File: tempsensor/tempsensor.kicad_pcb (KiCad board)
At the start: 4 copper layers, 40 x 40 mm, 68 parts, among them J1 Conn_01x14, J2 Conn_01x04, J3 Conn_ARM_JTAG_SWD_10, J4 USB_B_Micro, J5 Conn_01x02, SW1 SW_DIP_x06, SW2 PW_ON, SW4 ~INT, U1 MKW41Z512VHT, U2 24C16, U3 MCP9844, U4 SN74LVC2T45DCUR, U5 SN74LVC2T45DCUR, U6 BQ24012, Y1 32MHz 10PPM SMT 2.0x1.6mm 10PF, Y2 32.768KHz 20PPM 3.2x1.5mm 7PF

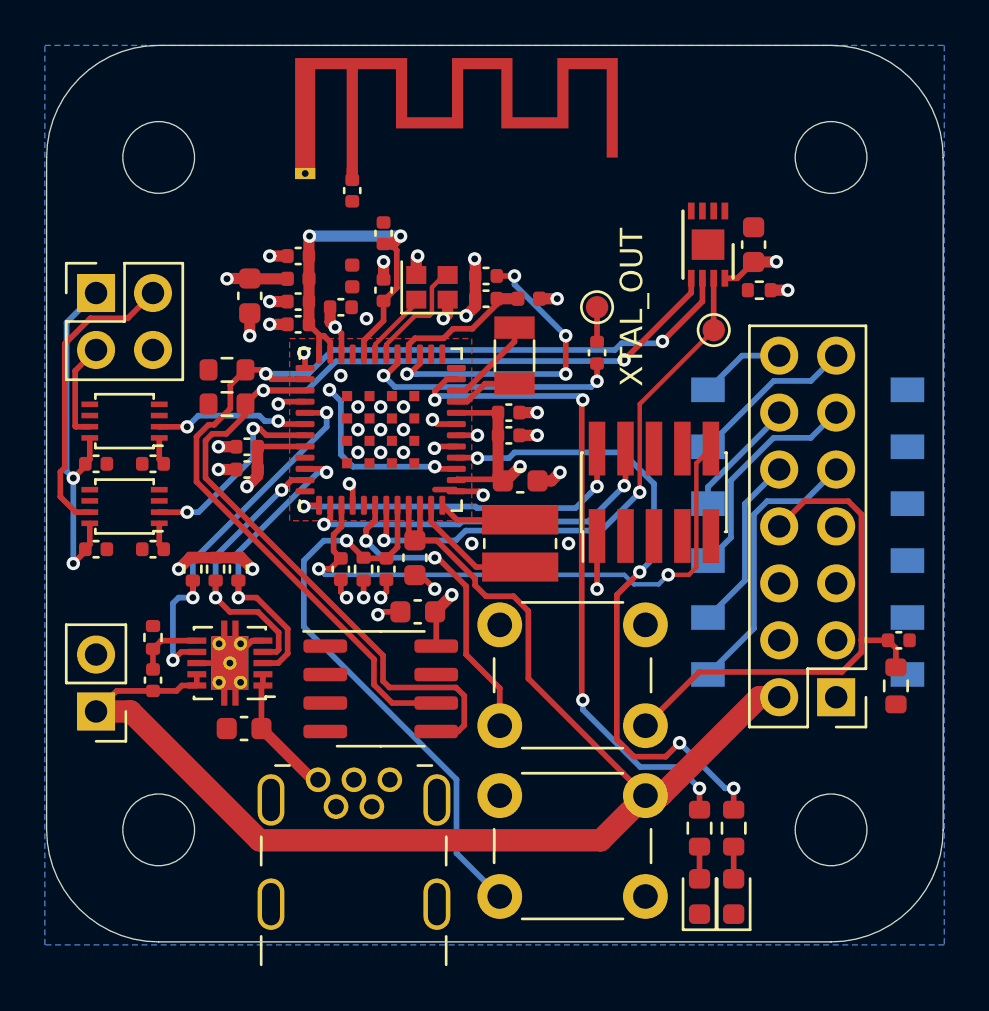
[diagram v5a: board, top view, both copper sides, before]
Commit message: Finished layouting tempsensor and thermostat. Parts are ordered from Mouser, PCB ordered from beta-layout.
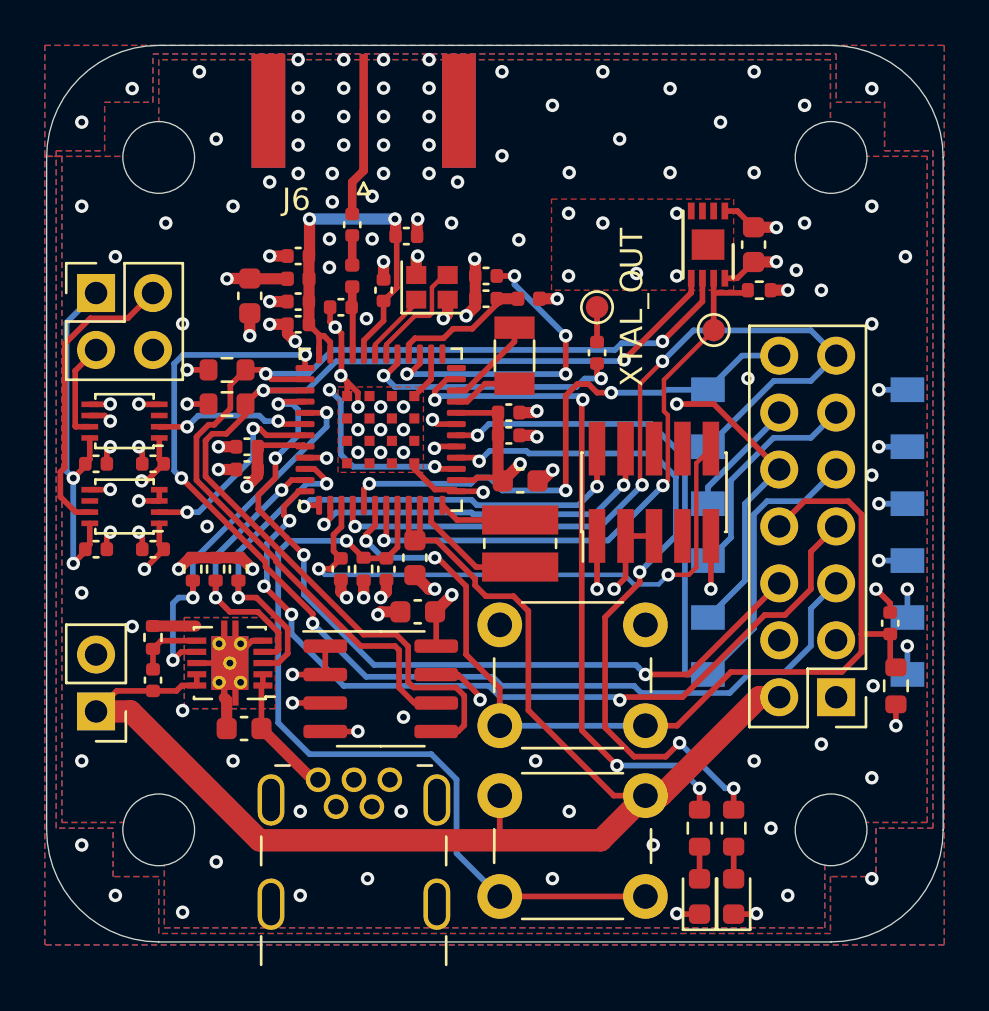
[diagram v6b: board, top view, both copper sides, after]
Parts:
- removed AE1: Antenna_Shield, RF_Antenna:Texas_SWRA117D_2.4GHz_Right
- added J6: Conn_Coaxial, Connector_Coaxial:SMA_Amphenol_132289_EdgeMount, F.Cu at (192.0, 71.5)
- moved C4 1.52 mm to (191.5, 76.6), turned to 270 degrees
- moved C29 1.02 mm to (193.9, 77.1), turned to 0 degrees
- moved C22 0.85 mm to (215.5, 94.4), turned to 90 degrees
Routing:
- net GND: track 25.7 -> 73.4 mm, vias 34 -> 149
- net /PTC1: track 0.70 -> 48.4 mm, vias 1 -> 3
- net /PTC19: track 0.00 -> 37.9 mm, vias 0 -> 4
- net /PTC4: track 1.24 -> 36.4 mm, vias 1 -> 4
- net /PTA16: track 8.43 -> 36.7 mm, vias 1 -> 3
- net /TMP0_CH3: track 5.38 -> 28.1 mm, vias 0 -> 1
- net /PTA17: track 3.81 -> 25.0 mm, vias 0 -> 3
- net /PTB2: track 13.4 -> 34.2 mm
- net /TMP0_CH2: track 11.0 -> 29.6 mm
- net /PTB3: track 9.07 -> 26.7 mm, vias 1 -> 2
- net Net-(C2-Pad1): track 25.6 -> 37.1 mm
- net /~BTN_INT: track 38.0 -> 44.8 mm
- net +1V8: track 27.6 -> 34.2 mm, vias 9 -> 15
- net Net-(C4-Pad1): track 0.00 -> 4.81 mm
- net Net-(C5-Pad1): track 0.00 -> 3.03 mm
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- added copper zone on In1.Cu, net GND
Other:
- net class RF added: clearance 0.2, trace_width 0.38276, via_dia 0.6, via_drill 0.3
